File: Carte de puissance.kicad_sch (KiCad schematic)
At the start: 91 parts, among them J1 5v external regulator, J2 other external regulator, J3 Pi_pwr, J4 Pi_data, J5 BAU1, J6 BAU2, J7 BAU3, J8 BAU4, J9 Programming, Q1 GSFP6901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

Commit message: Mise à jour de certains footprints
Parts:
- U10, U11, U12, U7, U9: footprint Package_DIP:DIP-4_W7.62mm -> Package_DIP:SMDIP-4_W11.48mm
- U8: value DPC817 -> DPC817-B; footprint Package_DIP:DIP-4_W7.62mm -> Package_DIP:SMDIP-4_W11.48mm
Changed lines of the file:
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@@
 			)
 		)
-		(property "Footprint" "Package_DIP:DIP-4_W7.62mm"
+		(property "Footprint" "Package_DIP:SMDIP-4_W11.48mm"
 			(at 25.4 162.56 0)
 			(hide yes)
@@
 			)
 		)
-		(property "Footprint" "Package_DIP:DIP-4_W7.62mm"
+		(property "Footprint" "Package_DIP:SMDIP-4_W11.48mm"
 			(at 25.4 114.3 0)
 			(hide yes)
@@
 			)
 		)
-		(property "Value" "DPC817"
+		(property "Value" "DPC817-B"
 			(at 106.68 114.3 0)
 			(show_name no)
@@
 			)
 		)
-		(property "Footprint" "Package_DIP:DIP-4_W7.62mm"
+		(property "Footprint" "Package_DIP:SMDIP-4_W11.48mm"
 			(at 111.76 125.73 0)
 			(hide yes)
@@
 			)
 		)
-		(property "Footprint" "Package_DIP:DIP-4_W7.62mm"
+		(property "Footprint" "Package_DIP:SMDIP-4_W11.48mm"
 			(at 25.4 138.43 0)
 			(hide yes)
@@
 			)
 		)
-		(property "Footprint" "Package_DIP:DIP-4_W7.62mm"
+		(property "Footprint" "Package_DIP:SMDIP-4_W11.48mm"
 			(at 109.22 107.95 0)
 			(hide yes)
@@
 			)
 		)
-		(property "Footprint" "Package_DIP:DIP-4_W7.62mm"
+		(property "Footprint" "Package_DIP:SMDIP-4_W11.48mm"
 			(at 25.4 186.69 0)
 			(hide yes)

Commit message: Placement des composants
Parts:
- F1, F2, F3, F4, F5: footprint (none) -> Fuse_custom:CONN_3557-2_KEY
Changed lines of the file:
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@@
 			)
 		)
-		(property "Footprint" ""
+		(property "Footprint" "Fuse_custom:CONN_3557-2_KEY"
 			(at 48.26 118.872 90)
 			(hide yes)
@@
 			)
 		)
-		(property "Footprint" ""
+		(property "Footprint" "Fuse_custom:CONN_3557-2_KEY"
 			(at 22.86 23.622 90)
 			(hide yes)
@@
 			)
 		)
-		(property "Footprint" ""
+		(property "Footprint" "Fuse_custom:CONN_3557-2_KEY"
 			(at 48.26 191.262 90)
 			(hide yes)
@@
 			)
 		)
-		(property "Footprint" ""
+		(property "Footprint" "Fuse_custom:CONN_3557-2_KEY"
 			(at 48.26 167.132 90)
 			(hide yes)
@@
 			)
 		)
-		(property "Footprint" ""
+		(property "Footprint" "Fuse_custom:CONN_3557-2_KEY"
 			(at 48.26 143.002 90)
 			(hide yes)

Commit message: Placement pour avoir une carte au format du module
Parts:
- added H1, H2, H3, H4: MountingHole, MountingHole:MountingHole_3.2mm_M3, symbol Mechanical:MountingHole

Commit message: début de routage
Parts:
- U13: footprint Package_DFN_QFN:VQFN-20-1EP_3x3mm_P0.4mm_EP1.7x1.7mm -> Package_SO:SSOP-20_5.3x7.2mm_P0.65mm
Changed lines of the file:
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@@
 			)
 		)
-		(property "Footprint" "Package_DFN_QFN:VQFN-20-1EP_3x3mm_P0.4mm_EP1.7x1.7mm"
+		(property "Footprint" "Package_SO:SSOP-20_5.3x7.2mm_P0.65mm"
 			(at 107.95 168.91 0)
 			(hide yes)

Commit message: Changement des empreintes de fusible
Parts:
- F1, F2, F3, F4, F5: footprint Fuse_custom:CONN_3557-2_KEY -> 3557-2_fuseholder:FUSE_3557_simple
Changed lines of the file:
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@@
 			)
 		)
-		(property "Footprint" "Fuse_custom:CONN_3557-2_KEY"
+		(property "Footprint" "3557-2_fuseholder:FUSE_3557_simple"
 			(at 48.26 118.872 90)
 			(hide yes)
@@
 			)
 		)
-		(property "Footprint" "Fuse_custom:CONN_3557-2_KEY"
+		(property "Footprint" "3557-2_fuseholder:FUSE_3557_simple"
 			(at 22.86 23.622 90)
 			(hide yes)
@@
 			)
 		)
-		(property "Footprint" "Fuse_custom:CONN_3557-2_KEY"
+		(property "Footprint" "3557-2_fuseholder:FUSE_3557_simple"
 			(at 48.26 191.262 90)
 			(hide yes)
@@
 			)
 		)
-		(property "Footprint" "Fuse_custom:CONN_3557-2_KEY"
+		(property "Footprint" "3557-2_fuseholder:FUSE_3557_simple"
 			(at 48.26 167.132 90)
 			(hide yes)
@@
 			)
 		)
-		(property "Footprint" "Fuse_custom:CONN_3557-2_KEY"
+		(property "Footprint" "3557-2_fuseholder:FUSE_3557_simple"
 			(at 48.26 143.002 90)
 			(hide yes)

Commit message: Ajout de l'empreinte des MR30PB
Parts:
- J1, J2: footprint (none) -> MR30PB:MR30PB
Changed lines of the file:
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@@
 			)
 		)
-		(property "Footprint" ""
+		(property "Footprint" "MR30PB:MR30PB"
 			(at 180.34 132.08 0)
 			(hide yes)
@@
 			)
 		)
-		(property "Footprint" ""
+		(property "Footprint" "MR30PB:MR30PB"
 			(at 242.57 133.35 0)
 			(hide yes)

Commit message: Routage V2 partiel
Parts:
- ALM1, ALM2, ALM3, ALM4: footprint Connector_Molex:Molex_Mini-Fit_Jr_5569-06A2_2x03_P4.20mm_Horizontal -> Molex:Molex_Mini-Fit_Jr_5569-06A2_2x03_P4.20mm_Horizontal
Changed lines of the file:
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@@
 		)
 	)
-	(global_label "VSENSE-"
-		(shape input)
-		(at 26.67 76.2 180)
-		(fields_autoplaced yes)
-		(effects
-			(font
-				(size 1.27 1.27)
-			)
-			(justify right)
-		)
-		(property "Intersheetrefs" "${INTERSHEET_REFS}"
-			(at 14.9763 76.2 0)
-			(hide yes)
-			(show_name no)
-			(do_not_autoplace no)
-			(effects
-				(font
-					(size 1.27 1.27)
-				)
-				(justify right)
-			)
-		)
-	)
 	(global_label "UPDI"
 		(shape input)
@@
 		)
 	)
-	(global_label "VSENSE-"
-		(shape input)
-		(at 139.7 25.4 270)
-		(fields_autoplaced yes)
-		(effects
-			(font
-				(size 1.27 1.27)
-			)
-			(justify right)
-		)
-		(property "Intersheetrefs" "${INTERSHEET_REFS}"
-			(at 139.7 37.0937 90)
-			(hide yes)
-			(show_name no)
-			(do_not_autoplace no)
-			(effects
-				(font
-					(size 1.27 1.27)
-				)
-				(justify right)
-			)
-		)
-	)
 	(global_label "EN_BATT"
 		(shape input)
@@
 			)
 		)
-		(property "Footprint" "Connector_Molex:Molex_Mini-Fit_Jr_5569-06A2_2x03_P4.20mm_Horizontal"
+		(property "Footprint" "Molex:Molex_Mini-Fit_Jr_5569-06A2_2x03_P4.20mm_Horizontal"
 			(at 58.42 166.37 0)
 			(hide yes)
@@
 			)
 		)
-		(property "Footprint" "Connector_Molex:Molex_Mini-Fit_Jr_5569-06A2_2x03_P4.20mm_Horizontal"
+		(property "Footprint" "Molex:Molex_Mini-Fit_Jr_5569-06A2_2x03_P4.20mm_Horizontal"
 			(at 58.42 190.5 0)
 			(hide yes)
@@
 	)
 	(symbol
+		(lib_id "power:+VSW")
+		(at 26.67 76.2 90)
+		(unit 1)
+		(body_style 1)
+		(exclude_from_sim no)
+		(in_bom yes)
+		(on_board yes)
+		(in_pos_files yes)
+		(dnp no)
+		(property "Reference" "#PWR094"
+			(at 30.48 76.2 0)
+			(hide yes)
+			(show_name no)
+			(do_not_autoplace no)
+			(effects
+				(font
+					(size 1.27 1.27)
+				)
+			)
+		)
+		(property "Value" "+VSW"
+			(at 23.622 76.2 90)
+			(show_name no)
+			(do_not_autoplace no)
+			(effects
+				(font
+					(size 1.27 1.27)
+				)
+				(justify left)
+			)
+		)
+		(property "Footprint" ""
+			(at 26.67 76.2 0)
+			(hide yes)
+			(show_name no)
+			(do_not_autoplace no)
+			(effects
+				(font
+					(size 1.27 1.27)
+				)
+			)
+		)
+		(property "Datasheet" ""
+			(at 26.67 76.2 0)
+			(hide yes)
+			(show_name no)
+			(do_not_autoplace no)
+			(effects
+				(font
+					(size 1.27 1.27)
+				)
+			)
+		)
+		(property "Description" "Power symbol creates a global label with name \"+VSW\""
+			(at 26.67 76.2 0)
+			(hide yes)
+			(show_name no)
+			(do_not_autoplace no)
+			(effects
+				(font
+					(size 1.27 1.27)
+				)
+			)
+		)
+		(pin "1"
+		)
+		(instances
+			(project "Carte de puissance"
+				(path "/11c20516-946c-4711-af8c-f1da2c6f5a05"
+					(reference "#PWR094")
+					(unit 1)
+				)
+			)
+		)
+	)
+	(symbol
 		(lib_id "power:VCC")
 		(at 68.58 73.66 0)
@@
 			)
 		)
-		(property "Footprint" "Connector_Molex:Molex_Mini-Fit_Jr_5569-06A2_2x03_P4.20mm_Horizontal"
+		(property "Footprint" "Molex:Molex_Mini-Fit_Jr_5569-06A2_2x03_P4.20mm_Horizontal"
 			(at 58.42 142.24 0)
 			(hide yes)
@@
 			)
 		)
-		(property "Footprint" "Connector_Molex:Molex_Mini-Fit_Jr_5569-06A2_2x03_P4.20mm_Horizontal"
+		(property "Footprint" "Molex:Molex_Mini-Fit_Jr_5569-06A2_2x03_P4.20mm_Horizontal"
 			(at 58.42 118.11 0)
 			(hide yes)

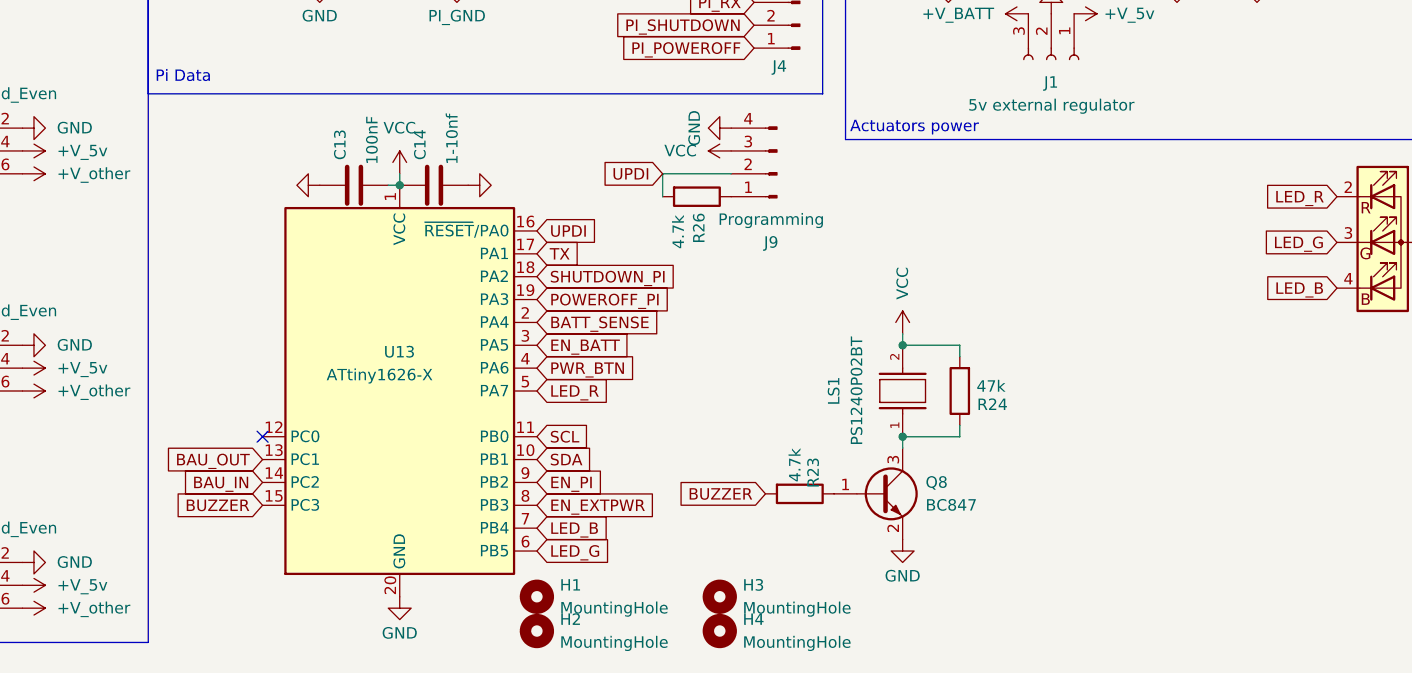
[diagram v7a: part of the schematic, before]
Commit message: Routage V2 signaux fini Il reste encore la puissance à finir
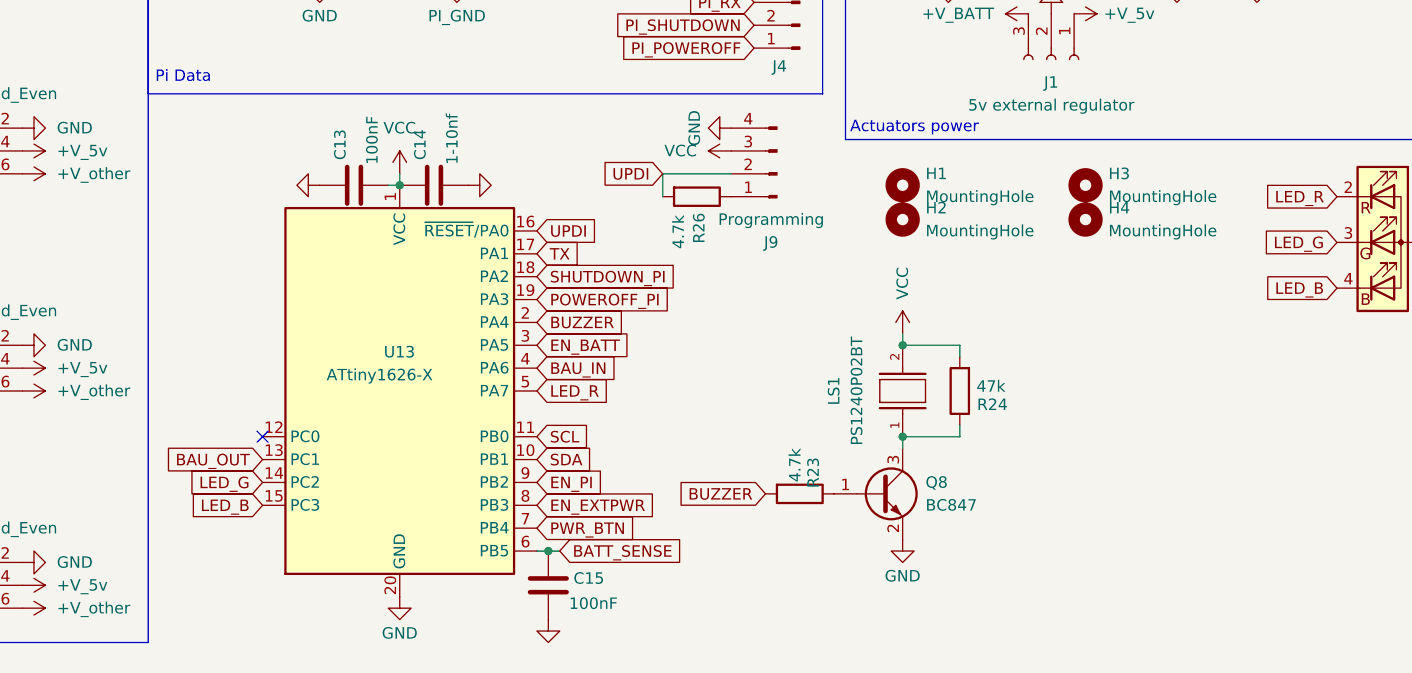
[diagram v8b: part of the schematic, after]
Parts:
- added C15: 100nF, Capacitor_SMD:C_0805_2012Metric, symbol Device:C
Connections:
- net BATT_SENSE: now also U13.6 (PB5), C15.1; no longer U13.2 (PA4)
- net BAU_IN: now also U13.4 (PA6); no longer U13.14 (PC2)
- net BUZZER: now also U13.2 (PA4); no longer U13.15 (PC3)
- net GND: now also C15.2
- net LED_B: now also U13.15 (PC3); no longer U13.7 (PB4)
- net LED_G: now also U13.14 (PC2); no longer U13.6 (PB5)
- net PWR_BTN: now also U13.7 (PB4); no longer U13.4 (PA6)
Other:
- moved on the sheet: H1, H2, H3, H4
